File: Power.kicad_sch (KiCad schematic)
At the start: 4 parts, among them M14 Module-power_12and5V-0.3, M8 Module-power_12and5V-0.3, P32 PG_5VP_APS

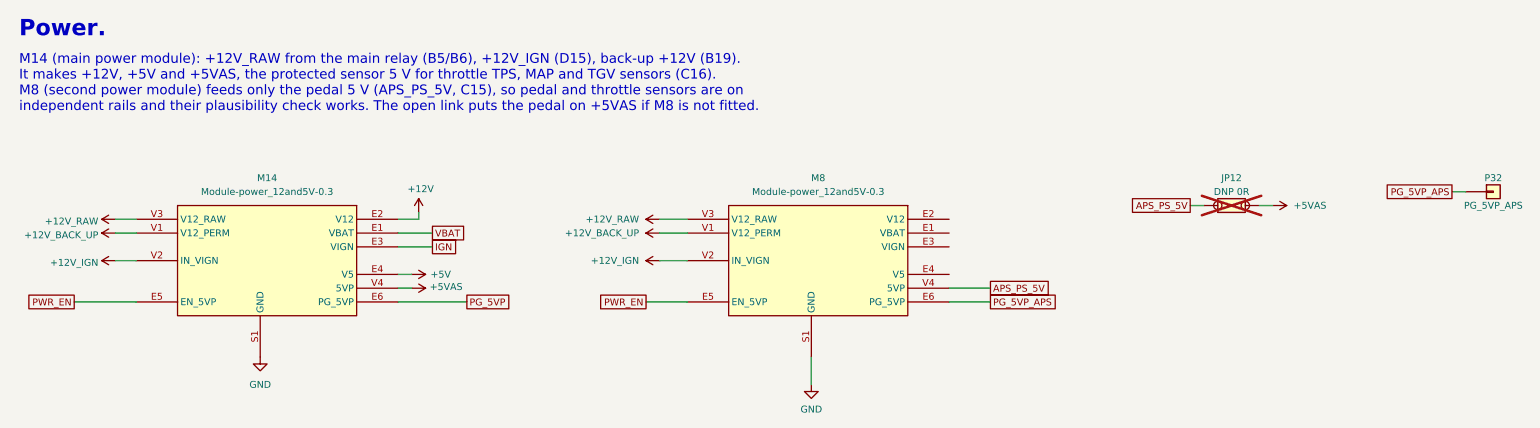
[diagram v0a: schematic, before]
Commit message: EmbeddedEra libraries and template, KiCad 10
- Every symbol except the nine Hellen-One modules now comes from the EmbeddedEra library (resistors and 0R links from the generic libraries, PTC fuses, VND14NV04-E, TE 1-1376430-0, Molex 39281143, test pads, proto area, power symbols). Same-pin parts swapped in place; resistors re-placed between their old pin points with short wires. New parts live on library branch sti2004-parts.
- EmbeddedEra project template: worksheet, text variables, net classes with explicit power classes, JLCPCB design rules; template net names for USB, I2C and the K-line UART.
- Migrated all sheets and the board to KiCad 10 (10.0.7).
- tools/sch_overlap_check.py also fails on overlapping symbol bodies and on fields printed across a wire (found the stacked PTC fuses); KiCad 10 hide flags understood.

Verified: connectivity identical to the previous commit (167 nets), only the planned net renames; 0 overlaps on all 10 sheet files; ERC errors unchanged (148); pinout check 99 OK.

Co-Authored-By: Claude Opus 5.5 <noreply@anthropic.com>
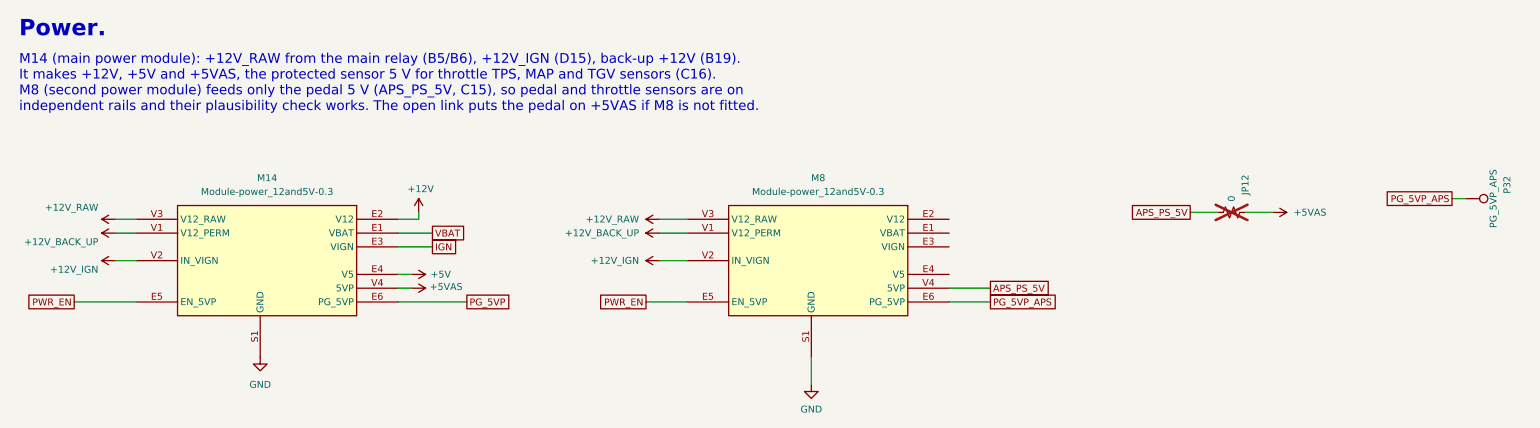
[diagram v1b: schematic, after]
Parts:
- removed JP12: DNP 0R, hellen-one-common:PAD-0805-PAD, symbol hellen-one-common:Jumper-Pad-Pad
- removed P32: PG_5VP_APS, hellen-one-common:PAD-TH, symbol hellen-one-common:Pad
- added JP12: 0, EmbeddedEra_Library:R_0805_2012Metric, symbol EmbeddedEra_Resistors_0805_5pct:EE_R_0805_0_5%
- added P32: PG_5VP_APS, EmbeddedEra_Library:TestPoint_THTPad_D2.0mm_Drill1.0mm, symbol EmbeddedEra:TestPoint_THT
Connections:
- net +5VAS: now also JP12.2
- net APS_PS_5V: now also JP12.1
- net PG_5VP_APS: now also P32.1
